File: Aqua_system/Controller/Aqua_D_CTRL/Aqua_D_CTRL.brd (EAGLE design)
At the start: 150 x 120 mm, 234 parts, among them IC1 SN65HVD3082EDR, IC2 CSTNE8M00G520000R0, IC3 LT6106CS5#TRPBF, IC4 LT6106CS5#TRPBF, IC5 TPS54202DDCR, IC6 LD1117S33TR, IC8 LM317AEMP, J1 ESP32-PICO-KIT, K1 KB20C06A, K2 KB20C06A, Q1 DMP6185SEQ-13, Q10 BC817, Q11 2N7002, Q12 DMP6185SEQ-13, Q13 2N7002, Q14 DMP6185SEQ-13, Q15 2N7002, Q16 DMP6185SEQ-13, Q17 BC817, Q18 BC817, Q19 BC817, Q2 2N7002, Q20 BC817, Q21 BC817, Q22 BC817, Q23 BC817, Q3 DMP6185SEQ-13, Q4 2N7002, Q5 DMP6185SEQ-13, Q6 DMP6185SEQ-13, Q7 2N7002, Q8 DMP6185SEQ-13, Q9 2N7002, SW1 L101011MS02Q, U2 R7FA6M5BG3CFBLQFP-144-M, X1 B2B-XH-AM(LF)(SN), X10 726386-2TE_726386-2, X11 282834-2, X12 615008148521, X13 MICROMATCH-16, X14 615008148521, X2 WF2549-2WS05S0B01, X3 282834-3, X4 282834-3, X5 726386-2TE_726386-2, X6 726386-2TE_726386-2, X7 726386-2TE_726386-2, X8 726386-2TE_726386-2, X9 726386-2TE_726386-2

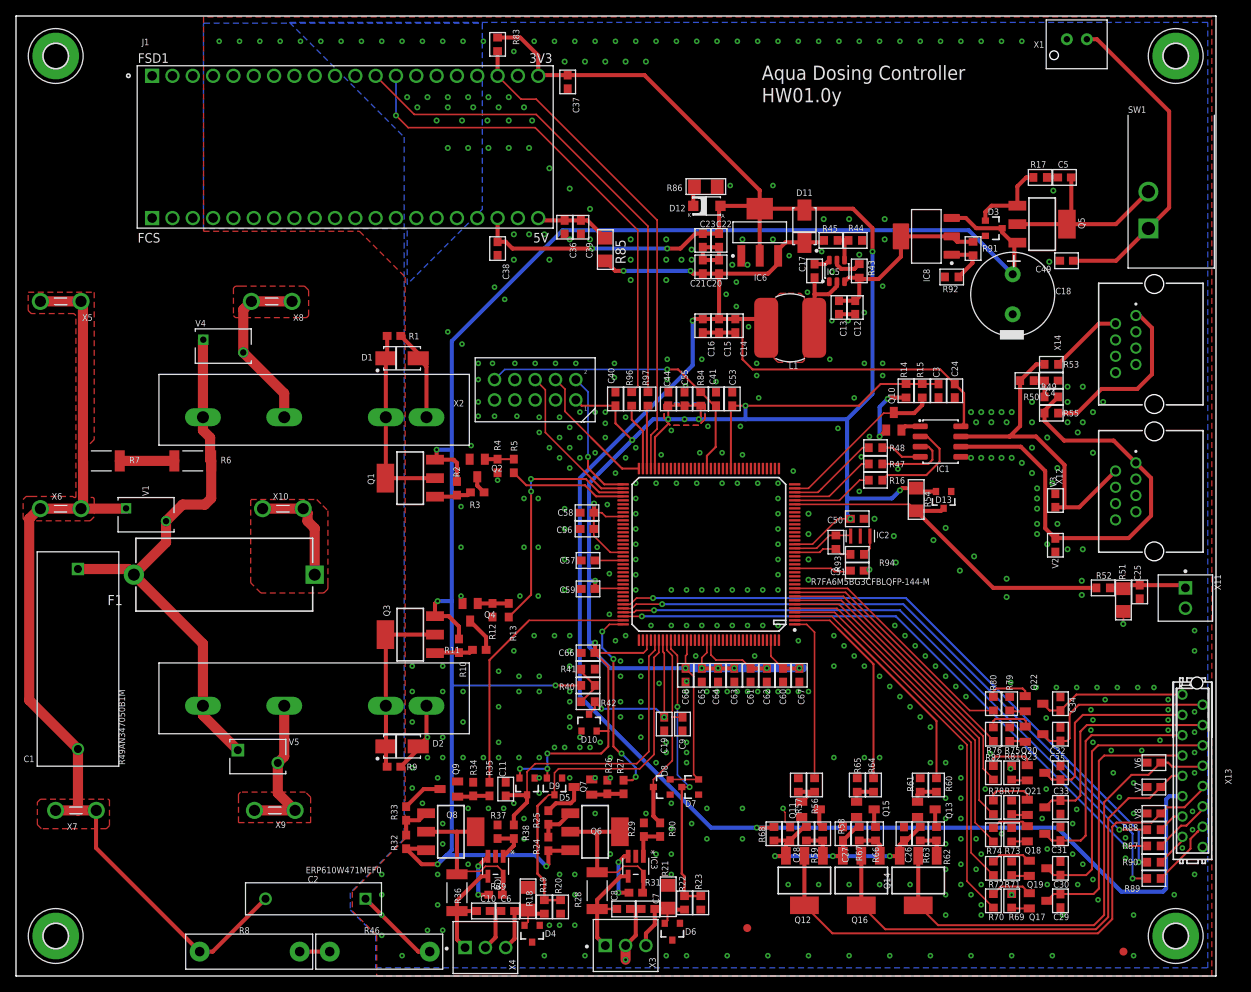
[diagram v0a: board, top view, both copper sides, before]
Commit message: HW02.02
Improvements after HW Functional Testing
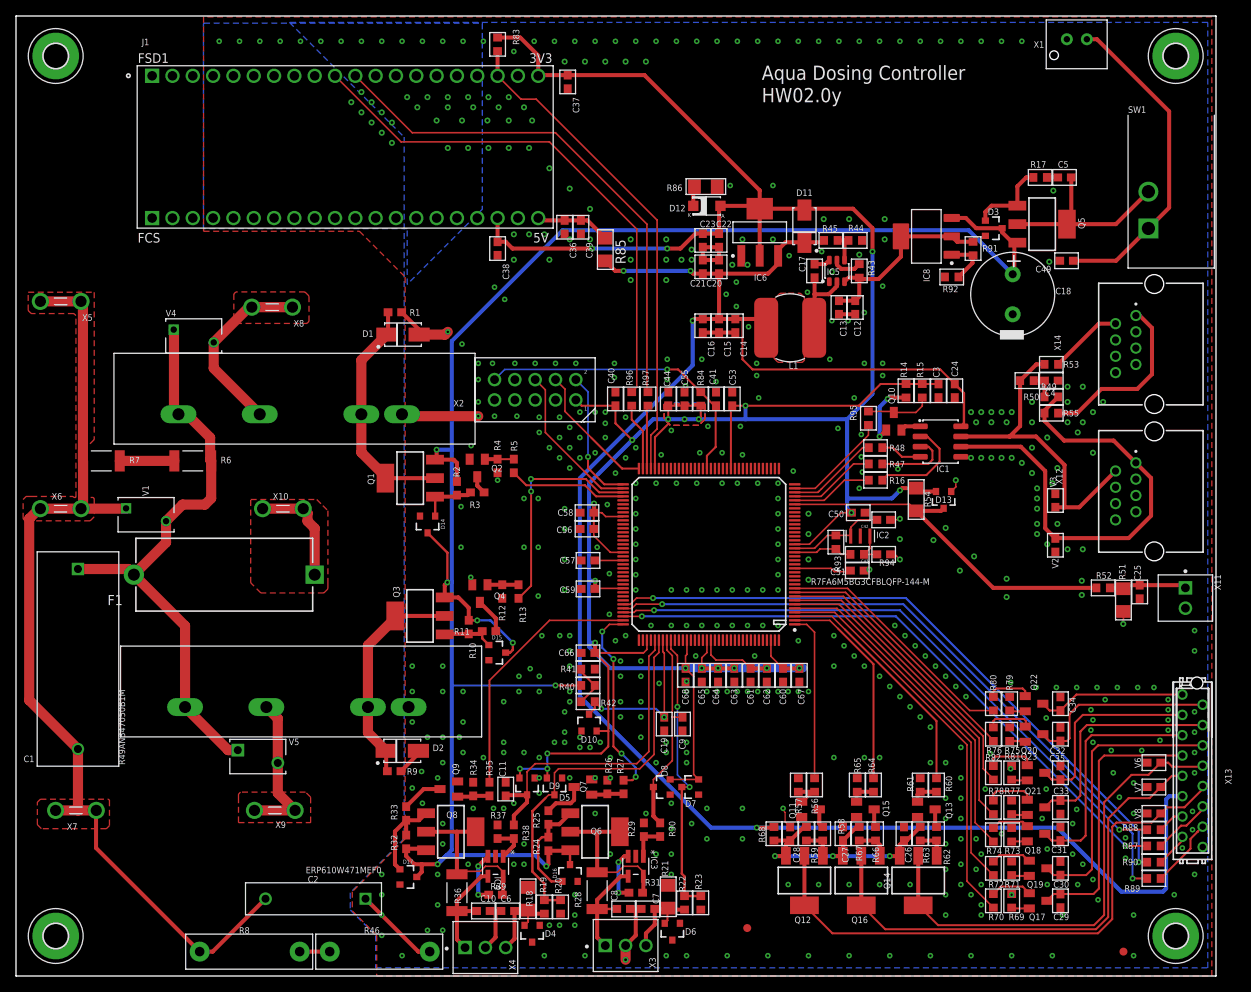
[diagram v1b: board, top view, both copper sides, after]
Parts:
- removed K2: KB20C06A, Labops_Lib_AH:RELAY_KYOTO_KF0604D
- added C42, C43: 10pF/100V, Labops_Lib_AH:0603
- added D14, D15, D16, D17: MMBZ4696-HE3-18, Labops_Lib_AH:SOT23-3
- added K3: RP1A48D6, Labops_Lib_AH:SSR_RP1A
- added R95: 470R 1%, Labops_Lib_AH:R0603
- K1: value KB20C06A -> RP1A48D6; device Labops_Lib_AH:RELAY_KYOTO_KF0604D -> Labops_Lib_AH:SSR_RP1A
- Q1, Q12, Q14, Q16, Q3, Q6, Q8: value DMP6185SEQ-13 -> UT2955G-AA3-R
- R58, R62, R66: value 10K 1% -> 100R 1%
- moved V4 3.90 mm to (22.2, 80.0)
- moved K1 3.08 mm to (48.2, 70.2)
- moved D1 2.96 mm to (48.4, 80.2)
- moved R1 2.96 mm to (47.4, 83.0)
- moved R10 2.64 mm to (56.6, 43.6)
- moved R12 2.64 mm to (60.8, 48.1)
- moved R13 2.64 mm to (62.8, 48.1)
- moved Q3 2.64 mm to (50.5, 45.0)
- moved Q4 2.64 mm to (58.0, 47.8)
- moved R11 2.64 mm to (59.1, 43.1)
- moved C50 0.77 mm to (105.3, 57.9)
- moved X8 0.73 mm to (32.0, 83.6)
- moved D2 0.56 mm to (48.3, 28.1)
- moved R9 0.56 mm to (47.3, 25.6)
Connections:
- removed net ESP32_RXD: J1.J2_12, R97.2
- removed net ESP32_TXD: J1.J2_13, R96.2
- new net ESP32_RXD1: J1.J2_11, R97.2
- new net ESP32_TXD1: J1.J2_10, R96.2
- new net N$59: Q10.3, R15.1, R95.1
- net CONDUCTIV_PUMP_MAINS_L_SW: now also K3.P$3; no longer K2.P$3
- net DI_USART_RX: now also R95.2; no longer Q10.3, R15.1
- net DO_7XSEGMENT_1_EN: now also R60.1, U2.3; no longer R56.1, U2.1
- net DO_7XSEGMENT_3_EN: now also R56.1, U2.1; no longer R60.1, U2.3
- net GND: now also C42.1, C43.1, K3.P$1; no longer K2.P$1
- net MAINS_L_F: now also K3.P$4; no longer K2.P$4
- net N$11: now also D15.1
- net N$13: now also D16.1
- net N$21: now also D17.1
- net N$3: now also D14.1
- net N$49: now also C43.2
- net N$5: now also K3.P$2; no longer K2.P$2
- net N$66: now also C42.2
- net V_24V0_P: now also D14.3, D15.3, D16.3, D17.3
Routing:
- net ESP32_TXD1: track 0.00 -> 66.3 mm
- net ESP32_RXD1: track 0.00 -> 65.2 mm
- net ESP32_RXD: track 62.6 -> 0.00 mm
- net ESP32_TXD: track 61.7 -> 0.00 mm, vias 1 -> 0
- net V_24V0_P: track 218.5 -> 237.3 mm, vias 5 -> 7
- net DO_7XSEGMENT_3_EN: track 30.3 -> 21.1 mm
- net DO_7XSEGMENT_1_EN: track 21.1 -> 30.3 mm
- net N$13: track 4.92 -> 13.5 mm
- net N$59: track 0.00 -> 8.17 mm
- net DI_USART_RX: track 21.3 -> 13.2 mm
- net N$21: track 4.71 -> 11.7 mm
- net N$1: track 24.1 -> 30.0 mm
- net N$5: track 22.8 -> 28.2 mm
- net N$66: track 7.70 -> 12.5 mm
- net GND: track 64.4 -> 68.8 mm, vias 528 -> 537
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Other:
- board text added: "HW02.0y"
- board text removed: "HW01.0y"
